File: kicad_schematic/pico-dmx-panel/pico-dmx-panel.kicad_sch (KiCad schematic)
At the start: 6 parts, among them SW1 WORK, SW2 RUN, SW3 OFF, U1 MAX485

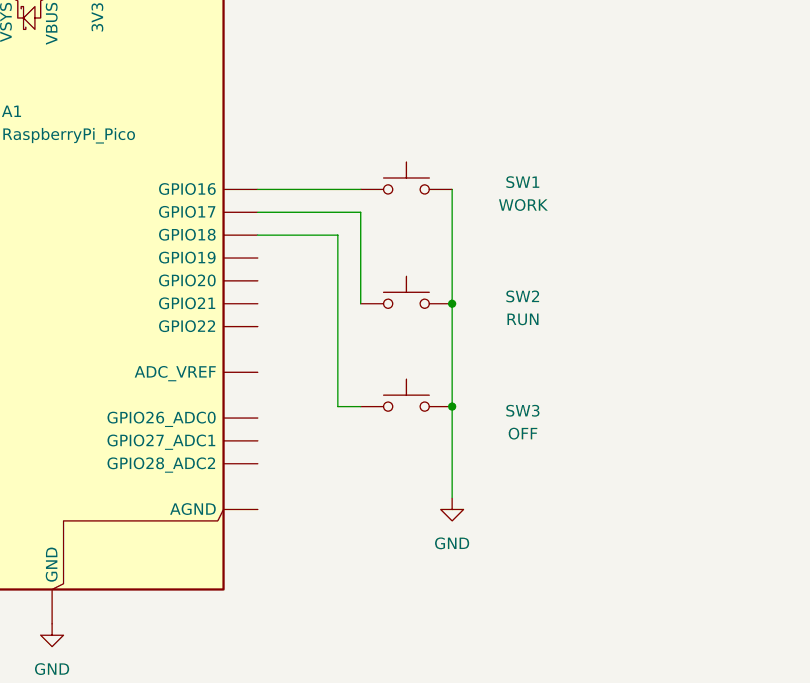
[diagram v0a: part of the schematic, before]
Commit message: update pinout in schematic
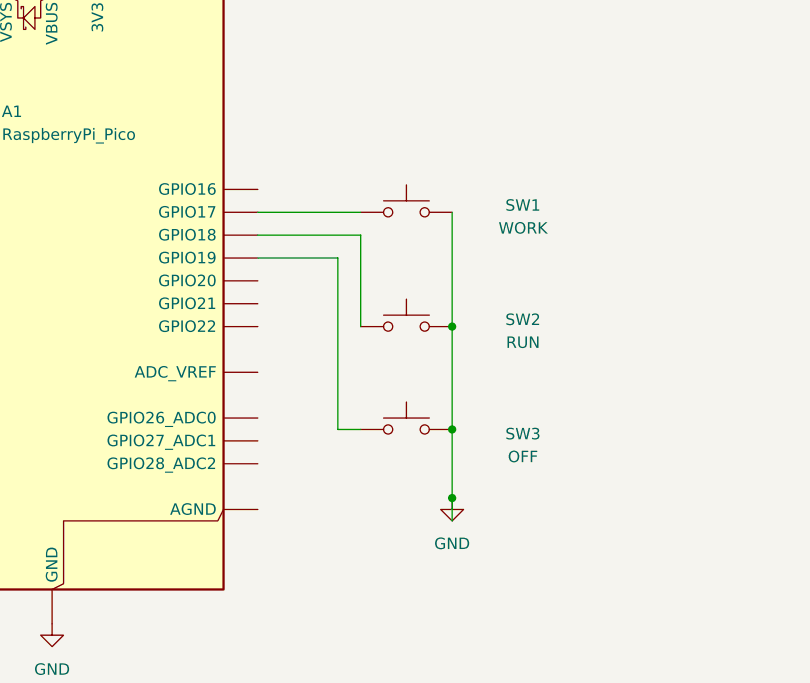
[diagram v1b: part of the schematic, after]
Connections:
- net at SW1.1: now also A1.22 (GPIO17); no longer A1.21 (GPIO16)
- net at SW3.1: now also A1.25 (GPIO19); no longer A1.24 (GPIO18)
- net at SW2.1: now also A1.24 (GPIO18); no longer A1.22 (GPIO17)
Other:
- moved on the sheet: SW1, SW2, SW3
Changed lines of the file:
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@@
 	)
 	(junction
-		(at 189.23 95.25)
+		(at 189.23 97.79)
 		(diameter 0)
 		(color 0 0 0 0)
 	)
 	(junction
-		(at 189.23 106.68)
+		(at 189.23 116.84)
 		(diameter 0)
 		(color 0 0 0 0)
 	)
+	(junction
+		(at 189.23 109.22)
+		(diameter 0)
+		(color 0 0 0 0)
+	)
 	(wire
 		(pts
@@
 	(wire
 		(pts
-			(xy 189.23 82.55) (xy 189.23 95.25)
-		)
-		(stroke
-			(width 0)
-			(type default)
-		)
-	)
-	(wire
-		(pts
-			(xy 176.53 106.68) (xy 176.53 87.63)
-		)
-		(stroke
-			(width 0)
-			(type default)
-		)
-	)
-	(wire
-		(pts
-			(xy 179.07 95.25) (xy 179.07 85.09)
+			(xy 189.23 85.09) (xy 189.23 97.79)
+		)
+		(stroke
+			(width 0)
+			(type default)
+		)
+	)
+	(wire
+		(pts
+			(xy 176.53 109.22) (xy 176.53 90.17)
+		)
+		(stroke
+			(width 0)
+			(type default)
+		)
+	)
+	(wire
+		(pts
+			(xy 179.07 97.79) (xy 179.07 87.63)
 		)
 		(stroke
@@
 	(wire
 		(pts
-			(xy 167.64 82.55) (xy 179.07 82.55)
+			(xy 167.64 85.09) (xy 179.07 85.09)
 		)
 		(stroke
@@
 	(wire
 		(pts
-			(xy 176.53 106.68) (xy 179.07 106.68)
-		)
-		(stroke
-			(width 0)
-			(type default)
-		)
-	)
-	(wire
-		(pts
-			(xy 179.07 85.09) (xy 167.64 85.09)
+			(xy 176.53 109.22) (xy 179.07 109.22)
+		)
+		(stroke
+			(width 0)
+			(type default)
+		)
+	)
+	(wire
+		(pts
+			(xy 179.07 87.63) (xy 167.64 87.63)
+		)
+		(stroke
+			(width 0)
+			(type default)
+		)
+	)
+	(wire
+		(pts
+			(xy 189.23 119.38) (xy 189.23 116.84)
 		)
 		(stroke
@@
 	(wire
 		(pts
-			(xy 189.23 95.25) (xy 189.23 106.68)
+			(xy 189.23 97.79) (xy 189.23 109.22)
 		)
 		(stroke
@@
 	(wire
 		(pts
-			(xy 176.53 87.63) (xy 167.64 87.63)
+			(xy 176.53 90.17) (xy 167.64 90.17)
 		)
 		(stroke
@@
 	(wire
 		(pts
-			(xy 189.23 106.68) (xy 189.23 116.84)
+			(xy 189.23 109.22) (xy 189.23 116.84)
 		)
 		(stroke
@@
 	(symbol
 		(lib_id "Switch:SW_Push")
-		(at 184.15 82.55 0)
+		(at 184.15 85.09 0)
 		(unit 1)
 		(exclude_from_sim no)
@@
 		(dnp no)
 		(property "Reference" "SW1"
-			(at 197.104 81.788 0)
+			(at 197.104 84.328 0)
 			(effects
 				(font
@@
 		)
 		(property "Value" "WORK"
-			(at 197.104 84.328 0)
-			(effects
-				(font
-					(size 1.27 1.27)
-				)
-			)
-		)
-		(property "Footprint" ""
-			(at 184.15 77.47 0)
+			(at 197.104 86.868 0)
+			(effects
+				(font
+					(size 1.27 1.27)
+				)
+			)
+		)
+		(property "Footprint" ""
+			(at 184.15 80.01 0)
 			(effects
 				(font
@@
 		)
 		(property "Datasheet" "~"
-			(at 184.15 77.47 0)
+			(at 184.15 80.01 0)
 			(effects
 				(font
@@
 		)
 		(property "Description" "Push button switch, generic, two pins"
-			(at 184.15 82.55 0)
+			(at 184.15 85.09 0)
 			(effects
 				(font
@@
 	(symbol
 		(lib_id "Switch:SW_Push")
-		(at 184.15 106.68 0)
+		(at 184.15 109.22 0)
 		(unit 1)
 		(exclude_from_sim no)
@@
 		(dnp no)
 		(property "Reference" "SW3"
-			(at 197.104 107.188 0)
+			(at 197.104 109.728 0)
 			(effects
 				(font
@@
 		)
 		(property "Value" "OFF"
-			(at 197.104 109.728 0)
-			(effects
-				(font
-					(size 1.27 1.27)
-				)
-			)
-		)
-		(property "Footprint" ""
-			(at 184.15 101.6 0)
+			(at 197.104 112.268 0)
+			(effects
+				(font
+					(size 1.27 1.27)
+				)
+			)
+		)
+		(property "Footprint" ""
+			(at 184.15 104.14 0)
 			(effects
 				(font
@@
 		)
 		(property "Datasheet" "~"
-			(at 184.15 101.6 0)
+			(at 184.15 104.14 0)
 			(effects
 				(font
@@
 		)
 		(property "Description" "Push button switch, generic, two pins"
-			(at 184.15 106.68 0)
+			(at 184.15 109.22 0)
 			(effects
 				(font
@@
 	(symbol
 		(lib_id "Switch:SW_Push")
-		(at 184.15 95.25 0)
+		(at 184.15 97.79 0)
 		(unit 1)
 		(exclude_from_sim no)
@@
 		(dnp no)
 		(property "Reference" "SW2"
-			(at 197.104 94.488 0)
+			(at 197.104 97.028 0)
 			(effects
 				(font
@@
 		)
 		(property "Value" "RUN"
-			(at 197.104 97.028 0)
-			(effects
-				(font
-					(size 1.27 1.27)
-				)
-			)
-		)
-		(property "Footprint" ""
-			(at 184.15 90.17 0)
+			(at 197.104 99.568 0)
+			(effects
+				(font
+					(size 1.27 1.27)
+				)
+			)
+		)
+		(property "Footprint" ""
+			(at 184.15 92.71 0)
 			(effects
 				(font
@@
 		)
 		(property "Datasheet" "~"
-			(at 184.15 90.17 0)
+			(at 184.15 92.71 0)
 			(effects
 				(font
@@
 		)
 		(property "Description" "Push button switch, generic, two pins"
-			(at 184.15 95.25 0)
-			(effects
-				(font
+			(at 184.15 97.79 0)
+			(effects
+				(font
